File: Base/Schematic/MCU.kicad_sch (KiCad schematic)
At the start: 19 parts, among them U1 MB85RC16PNF-G-JNE, U2 SL1307ZN+T, U3 M433LE8AE, X1 XKXGI-SUA-32.768K, X2 1532H4-12000JWPDTSNL

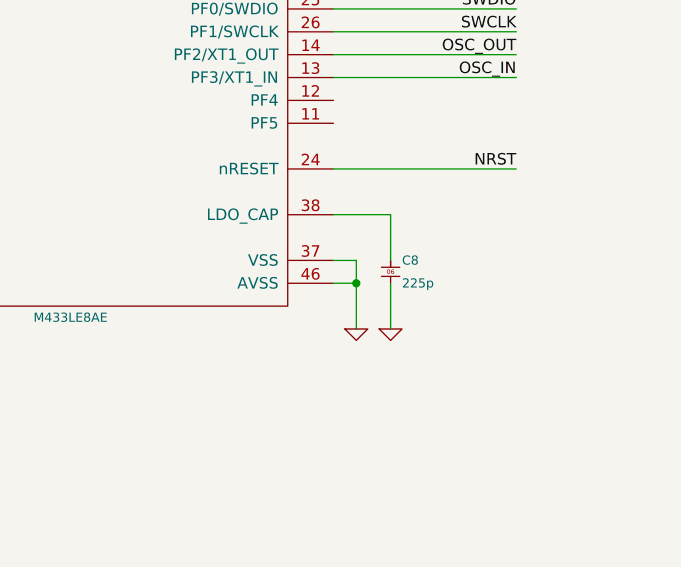
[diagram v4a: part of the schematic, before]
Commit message: [Base 회로도 업데이트] - AIN 입력 4개 추가
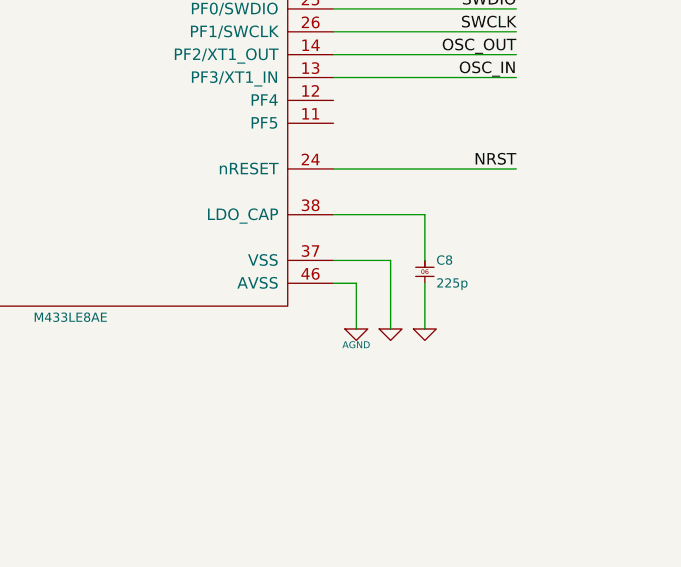
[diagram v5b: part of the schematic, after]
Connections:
- net GND: no longer U3.46 (AVSS)
- new net AGND: U3.46 (AVSS)
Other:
- company: (none) -> -
- title: (none) -> Open-PLC-Project
- moved on the sheet: C8
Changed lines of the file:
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@@
 	(paper "A4")
 	(title_block
+		(title "Open-PLC-Project")
+		(date "2024-12-01")
+		(company "-")
 		(comment 1 "See the file \"LICENSE\" in the main directory of this archive for more details.")
 		(comment 2 "This file is subject to the terms and conditions of the MIT License.")
@@
 	)
 	(junction
-		(at 176.53 124.46)
-		(diameter 0)
-		(color 0 0 0 0)
-	)
-	(junction
 		(at 53.34 173.99)
 		(diameter 0)
@@
 	(wire
 		(pts
-			(xy 176.53 121.92) (xy 176.53 124.46)
-		)
-		(stroke
-			(width 0)
-			(type default)
-		)
-	)
-	(wire
-		(pts
 			(xy 31.75 87.63) (xy 29.21 87.63)
 		)
@@
 	(wire
 		(pts
-			(xy 173.99 116.84) (xy 180.34 116.84)
+			(xy 173.99 116.84) (xy 184.15 116.84)
 		)
 		(stroke
@@
 	(wire
 		(pts
-			(xy 173.99 121.92) (xy 176.53 121.92)
+			(xy 173.99 121.92) (xy 180.34 121.92)
 		)
 		(stroke
@@
 	(wire
 		(pts
-			(xy 180.34 116.84) (xy 180.34 121.92)
+			(xy 184.15 116.84) (xy 184.15 121.92)
 		)
 		(stroke
@@
 	(wire
 		(pts
+			(xy 180.34 129.54) (xy 180.34 121.92)
+		)
+		(stroke
+			(width 0)
+			(type default)
+		)
+	)
+	(wire
+		(pts
 			(xy 34.29 148.59) (xy 22.86 148.59)
 		)
@@
 	(wire
 		(pts
-			(xy 180.34 124.46) (xy 180.34 129.54)
+			(xy 184.15 124.46) (xy 184.15 129.54)
 		)
 		(stroke
@@
 		(dnp no)
 		(fields_autoplaced yes)
-		(property "Reference" "#PWR019"
+		(property "Reference" "#PWR020"
 			(at 205.74 53.594 0)
 			(effects
@@
 			(project "Open-PLC-Project"
 				(path "/0d177ca6-e392-45a0-9514-d370436392ef/4500522c-e4c8-424c-82ea-be640253686b"
-					(reference "#PWR019")
+					(reference "#PWR020")
 					(unit 1)
 				)
@@
 	(symbol
 		(lib_id "power:GND")
+		(at 180.34 129.54 0)
+		(unit 1)
+		(exclude_from_sim no)
+		(in_bom yes)
+		(on_board yes)
+		(dnp no)
+		(fields_autoplaced yes)
+		(property "Reference" "#PWR016"
+			(at 180.34 129.54 0)
+			(effects
+				(font
+					(size 0.762 0.762)
+				)
+				(hide yes)
+			)
+		)
+		(property "Value" "GND"
+			(at 180.34 131.318 0)
+			(effects
+				(font
+					(size 0.762 0.762)
+				)
+				(hide yes)
+			)
+		)
+		(property "Footprint" ""
+			(at 180.34 129.54 0)
+			(effects
+				(font
+					(size 1.524 1.524)
+				)
+			)
+		)
+		(property "Datasheet" ""
+			(at 180.34 129.54 0)
+			(effects
+				(font
+					(size 1.524 1.524)
+				)
+			)
+		)
+		(property "Description" ""
+			(at 180.34 129.54 0)
+			(effects
+				(font
+					(size 1.27 1.27)
+				)
+				(hide yes)
+			)
+		)
+		(pin "1"
+		)
+		(instances
+			(project "Open-PLC-Project"
+				(path "/0d177ca6-e392-45a0-9514-d370436392ef/4500522c-e4c8-424c-82ea-be640253686b"
+					(reference "#PWR016")
+					(unit 1)
+				)
+			)
+		)
+	)
+	(symbol
+		(lib_id "power:GND")
 		(at 198.12 60.96 0)
 		(unit 1)
@@
 		(dnp no)
 		(fields_autoplaced yes)
-		(property "Reference" "#PWR018"
+		(property "Reference" "#PWR019"
 			(at 198.12 60.96 0)
 			(effects
@@
 			(project "Open-PLC-Project"
 				(path "/0d177ca6-e392-45a0-9514-d370436392ef/4500522c-e4c8-424c-82ea-be640253686b"
-					(reference "#PWR018")
+					(reference "#PWR019")
 					(unit 1)
 				)
@@
 		(dnp no)
 		(fields_autoplaced yes)
-		(property "Reference" "#PWR017"
+		(property "Reference" "#PWR018"
 			(at 198.12 53.594 0)
 			(effects
@@
 			(project "Open-PLC-Project"
 				(path "/0d177ca6-e392-45a0-9514-d370436392ef/4500522c-e4c8-424c-82ea-be640253686b"
-					(reference "#PWR017")
+					(reference "#PWR018")
 					(unit 1)
 				)
@@
 	)
 	(symbol
-		(lib_id "power:GND")
-		(at 176.53 129.54 0)
-		(unit 1)
-		(exclude_from_sim no)
-		(in_bom yes)
-		(on_board yes)
-		(dnp no)
-		(fields_autoplaced yes)
-		(property "Reference" "#PWR013"
-			(at 176.53 129.54 0)
-			(effects
-				(font
-					(size 0.762 0.762)
-				)
-				(hide yes)
-			)
-		)
-		(property "Value" "GND"
-			(at 176.53 131.318 0)
-			(effects
-				(font
-					(size 0.762 0.762)
-				)
-				(hide yes)
-			)
-		)
-		(property "Footprint" ""
-			(at 176.53 129.54 0)
-			(effects
-				(font
-					(size 1.524 1.524)
-				)
-			)
-		)
-		(property "Datasheet" ""
-			(at 176.53 129.54 0)
-			(effects
-				(font
-					(size 1.524 1.524)
-				)
-			)
-		)
-		(property "Description" ""
-			(at 176.53 129.54 0)
-			(effects
-				(font
-					(size 1.27 1.27)
-				)
-				(hide yes)
-			)
-		)
-		(pin "1"
-		)
-		(instances
-			(project "Open-PLC-Project"
-				(path "/0d177ca6-e392-45a0-9514-d370436392ef/4500522c-e4c8-424c-82ea-be640253686b"
-					(reference "#PWR013")
-					(unit 1)
-				)
-			)
-		)
-	)
-	(symbol
 		(lib_id "Capacitor_MLCC:0603X225K100")
-		(at 180.34 123.19 0)
+		(at 184.15 123.19 0)
 		(unit 1)
 		(exclude_from_sim no)
@@
 		(fields_autoplaced yes)
 		(property "Reference" "C8"
-			(at 181.61 121.92 0)
+			(at 185.42 121.92 0)
 			(do_not_autoplace yes)
 			(effects
@@
 		)
 		(property "Value" "0603X225K100"
-			(at 180.34 128.27 0)
+			(at 184.15 128.27 0)
 			(effects
 				(font
@@
 		)
 		(property "Footprint" "Capacitor_SMD:C_0603_1608Metric_Pad1.08x0.95mm_HandSolder"
-			(at 180.34 129.54 0)
+			(at 184.15 129.54 0)
 			(effects
 				(font
@@
 		)
 		(property "Datasheet" ""
-			(at 182.88 121.92 0)
+			(at 186.69 121.92 0)
 			(effects
 				(font
@@
 		)
 		(property "Description" "2.2uF 10% 10V X5R"
-			(at 180.34 130.81 0)
+			(at 184.15 130.81 0)
 			(effects
 				(font
@@
 		)
 		(property "Manufacturer" "WALSIN"
-			(at 180.34 127 0)
+			(at 184.15 127 0)
 			(effects
 				(font
@@
 		)
 		(property "#Value" "225p"
-			(at 181.61 124.46 0)
+			(at 185.42 124.46 0)
 			(do_not_autoplace yes)
 			(effects
@@
 		)
 		(property "Description_1" ""
-			(at 180.34 123.19 0)
+			(at 184.15 123.19 0)
 			(effects
 				(font
@@
 	(symbol
 		(lib_id "power:GND")
-		(at 180.34 129.54 0)
+		(at 184.15 129.54 0)
 		(unit 1)
 		(exclude_from_sim no)
@@
 		(dnp no)
 		(fields_autoplaced yes)
-		(property "Reference" "#PWR016"
-			(at 180.34 129.54 0)
+		(property "Reference" "#PWR017"
+			(at 184.15 129.54 0)
 			(effects
 				(font
@@
 		)
 		(property "Value" "GND"
-			(at 180.34 131.318 0)
+			(at 184.15 131.318 0)
 			(effects
 				(font
@@
 		)
 		(property "Footprint" ""
-			(at 180.34 129.54 0)
+			(at 184.15 129.54 0)
 			(effects
 				(font
@@
 		)
 		(property "Datasheet" ""
-			(at 180.34 129.54 0)
+			(at 184.15 129.54 0)
 			(effects
 				(font
@@
 		)
 		(property "Description" ""
-			(at 180.34 129.54 0)
+			(at 184.15 129.54 0)
 			(effects
 				(font
@@
 			(project "Open-PLC-Project"
 				(path "/0d177ca6-e392-45a0-9514-d370436392ef/4500522c-e4c8-424c-82ea-be640253686b"
-					(reference "#PWR016")
+					(reference "#PWR017")
 					(unit 1)
 				)
@@
 		(dnp no)
 		(fields_autoplaced yes)
-		(property "Reference" "#PWR020"
+		(property "Reference" "#PWR021"
 			(at 205.74 60.96 0)
 			(effects
@@
 			(project "Open-PLC-Project"
 				(path "/0d177ca6-e392-45a0-9514-d370436392ef/4500522c-e4c8-424c-82ea-be640253686b"
-					(reference "#PWR020")
+					(reference "#PWR021")
+					(unit 1)
+				)
+			)
+		)
+	)
+	(symbol
+		(lib_name "AGND_1")
+		(lib_id "power:AGND")
+		(at 176.53 129.54 0)
+		(unit 1)
+		(exclude_from_sim no)
+		(in_bom yes)
+		(on_board yes)
+		(dnp no)
+		(fields_autoplaced yes)
+		(property "Reference" "#PWR013"
+			(at 176.53 129.54 0)
+			(effects
+				(font
+					(size 0.762 0.762)
+				)
+				(hide yes)
+			)
+		)
+		(property "Value" "AGND"
+			(at 176.53 131.318 0)
+			(do_not_autoplace yes)
+			(effects
+				(font
+					(size 0.762 0.762)
+				)
+			)
+		)
+		(property "Footprint" ""
+			(at 176.53 129.54 0)
+			(effects
+				(font
+					(size 1.524 1.524)
+				)
+			)
+		)
+		(property "Datasheet" ""
+			(at 176.53 129.54 0)
+			(effects
+				(font
+					(size 1.524 1.524)
+				)
+			)
+		)
+		(property "Description" ""
+			(at 176.53 129.54 0)
+			(effects
+				(font
+					(size 1.27 1.27)
+				)
+				(hide yes)
+			)
+		)
+		(pin "1"
+		)
+		(instances
+			(project "Open-PLC-Project"
+				(path "/0d177ca6-e392-45a0-9514-d370436392ef/4500522c-e4c8-424c-82ea-be640253686b"
+					(reference "#PWR013")
 					(unit 1)
 				)
